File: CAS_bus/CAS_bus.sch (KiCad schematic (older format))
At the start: 1 part, among them J1 CAS_stacking

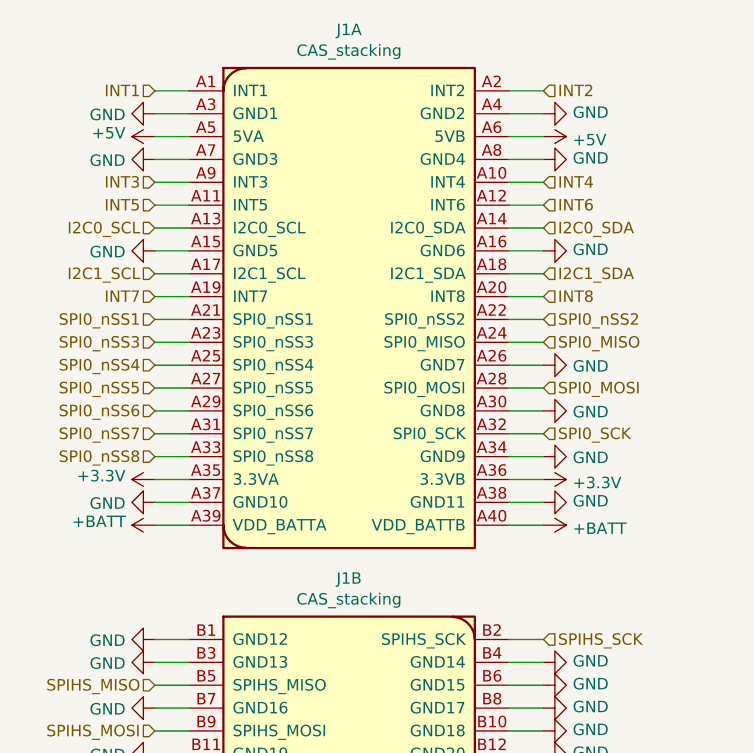
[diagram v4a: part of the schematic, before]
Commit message: add symbol libraries, and cleanup
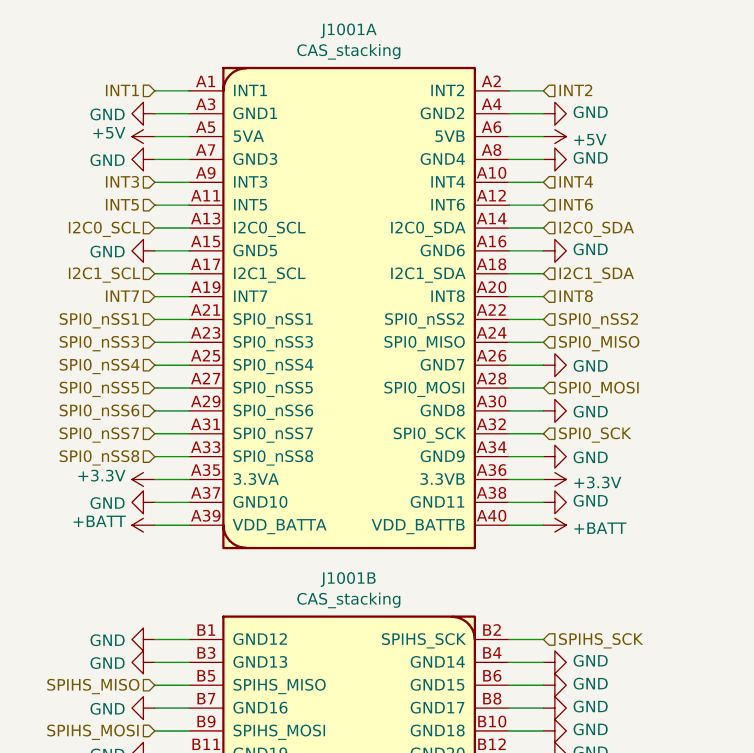
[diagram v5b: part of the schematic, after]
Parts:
- J1001: renamed from J1; footprint (none) -> star-common-lib:CAS_physical
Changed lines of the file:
@@
 $Descr A4 11693 8268
 encoding utf-8
-Sheet 1 6
+Sheet 1 1
 Title ""
 Date ""
@@
 SPI0_nSS1
 $Comp
-L star-common-lib:CAS_stacking J1
+L star-common-lib:CAS_stacking J1001
 U 1 1 5F2F934D
 P 5150 2750
-F 0 "J1" H 5150 3967 50  0000 C CNN
+F 0 "J1001" H 5150 3967 50  0000 C CNN
 F 1 "CAS_stacking" H 5150 3876 50  0000 C CNN
-F 2 "" H 5250 3700 50  0001 C CNN
+F 2 "star-common-lib:CAS_physical" H 5250 3700 50  0001 C CNN
 F 3 "" H 5250 3700 50  0001 C CNN
 	1    5150 2750
@@
 $EndComp
 $Comp
-L star-common-lib:CAS_stacking J1
+L star-common-lib:CAS_stacking J1001
 U 2 1 5F2FC6A4
 P 5150 5150
-F 0 "J1" H 5150 6367 50  0000 C CNN
+F 0 "J1001" H 5150 6367 50  0000 C CNN
 F 1 "CAS_stacking" H 5150 6276 50  0000 C CNN
-F 2 "" H 5250 6100 50  0001 C CNN
+F 2 "star-common-lib:CAS_physical" H 5250 6100 50  0001 C CNN
 F 3 "" H 5250 6100 50  0001 C CNN
 	2    5150 5150
